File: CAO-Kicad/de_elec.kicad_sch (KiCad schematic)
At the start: 17 parts, among them J1 ICSP, SW1 COMMUTATEUR VIBRATION, U1 puce de microcontrôleur IC AT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

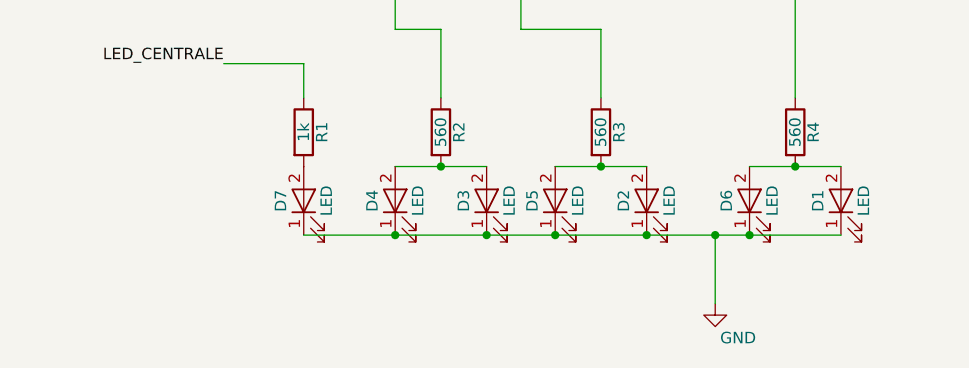
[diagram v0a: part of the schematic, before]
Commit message: Ajout de la serigraphie et recherche composants
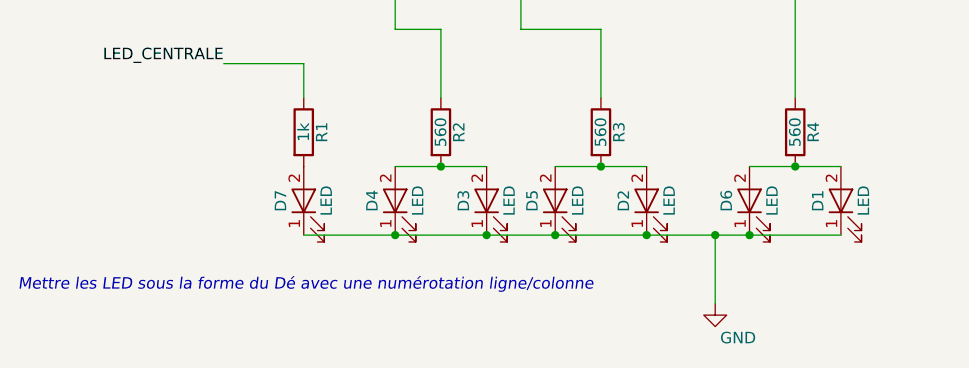
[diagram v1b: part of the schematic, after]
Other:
- note added: "Mettre les LED sous la forme du Dé avec une numérotation ligne/colonne"
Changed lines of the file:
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@@
     (stroke (width 0) (type solid) (color 0 0 0 0))
+  )
+  (text "Mettre les LED sous la forme du Dé avec une numérotation ligne/colonne"
+    (at 24.13 143.51 0)
+    (effects (font (size 1.27 1.27) italic) (justify left bottom))
   )
   (label "LED_CENTRALE" (at 46.99 118.11 180)

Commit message: Ajout des docs et images
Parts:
- removed D1, D2, D3, D4, D5, D6, D7: LED, LEDs:LED_D5.0mm, symbol kicad_dÚ-rescue:LED
- removed JP1: Jumper_2_Open, symbol Jumper:Jumper_2_Open
- removed R1: 1k, Resistors_SMD:R_0805_HandSoldering, symbol kicad_dÚ-rescue:R
- removed R2, R3, R4: 560, Resistors_SMD:R_0805_HandSoldering, symbol kicad_dÚ-rescue:R
- removed SW1: COMMUTATEUR VIBRATION, Capacitors_THT:CP_Radial_D5.0mm_P2.50mm, symbol kicad_dÚ-rescue:SW_SPST
- removed U1: puce de microcontrôleur IC ATTINY85 MCU 8BIT ATTI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, Housings_DIP:DIP-8_W7.62mm, symbol kicad_dÚ-rescue:ATTINY85-20PU
- added BT1: Battery_Cell_3V, symbol Device:Battery_Cell
- added D_L1C1, D_L1C3, D_L2C1, D_L2C2, D_L2C3, D_L3C1, D_L3C3: LED, symbol Device:LED
- added R1: 1k, symbol Device:R
- added R2, R3, R4: 560, symbol Device:R
- added SW1: COMMUTATEUR A BILLE, Capacitors_THT:CP_Radial_D5.0mm_P2.50mm, symbol Switch:SW_SPST
- added U1: ATtiny85V-10P, Package_DIP:DIP-8_W7.62mm, symbol MCU_Microchip_ATtiny:ATtiny85V-10P
- C1: value C -> 100n
- C2: value C_Polarized -> 10u
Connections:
- net GND: now also BT1.2 (-), D_L1C1.1 (K), D_L1C3.1 (K), D_L2C1.1 (K), D_L2C2.1 (K), D_L2C3.1 (K), D_L3C1.1 (K), D_L3C3.1 (K), SW1.2 (B), U1.4 (GND)
- net PB0/MOSI: now also R3.1, U1.5 (AREF/PB0)
- net PB1/MISO: now also R2.1, U1.6 (PB1)
- net PB2/SCK: now also SW1.1 (A), U1.7 (PB2)
- net PB5/RESET: now also U1.1 (~{RESET}/PB5)
- net VCC: now also BT1.1 (+), U1.8 (VCC)
- new net: R4.2, U1.3 (XTAL2/PB4)
- new net CMD_L2C2: R1.1, U1.2 (XTAL1/PB3)
- new net D_L1C1L3C3: D_L1C1.2 (A), D_L3C3.2 (A), R3.2
- new net D_L2C1C3: D_L2C1.2 (A), D_L2C3.2 (A), R4.1
- new net D_L2C2: D_L2C2.2 (A), R1.2
- new net D_L3C1L1C3: D_L1C3.2 (A), D_L3C1.2 (A), R2.2
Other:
- note added: "Carte microcontrôleur ATtiny85"
- note added: "Disposition des LED sous la forme du Dé avec une numérotation ligne/colonne"
- note added: "L1C1"
- note added: "L1C2"
- note added: "L1C3"
- note added: "L2C1"
- note added: "L2C2"
- note added: "L2C3"
- note added: "L3C1"
- note added: "L3C2"
- note added: "L3C3"
- note removed: "Mettre les LED sous la forme du Dé avec une numérotation ligne/colonne"
- moved on the sheet: C1, C2, J1

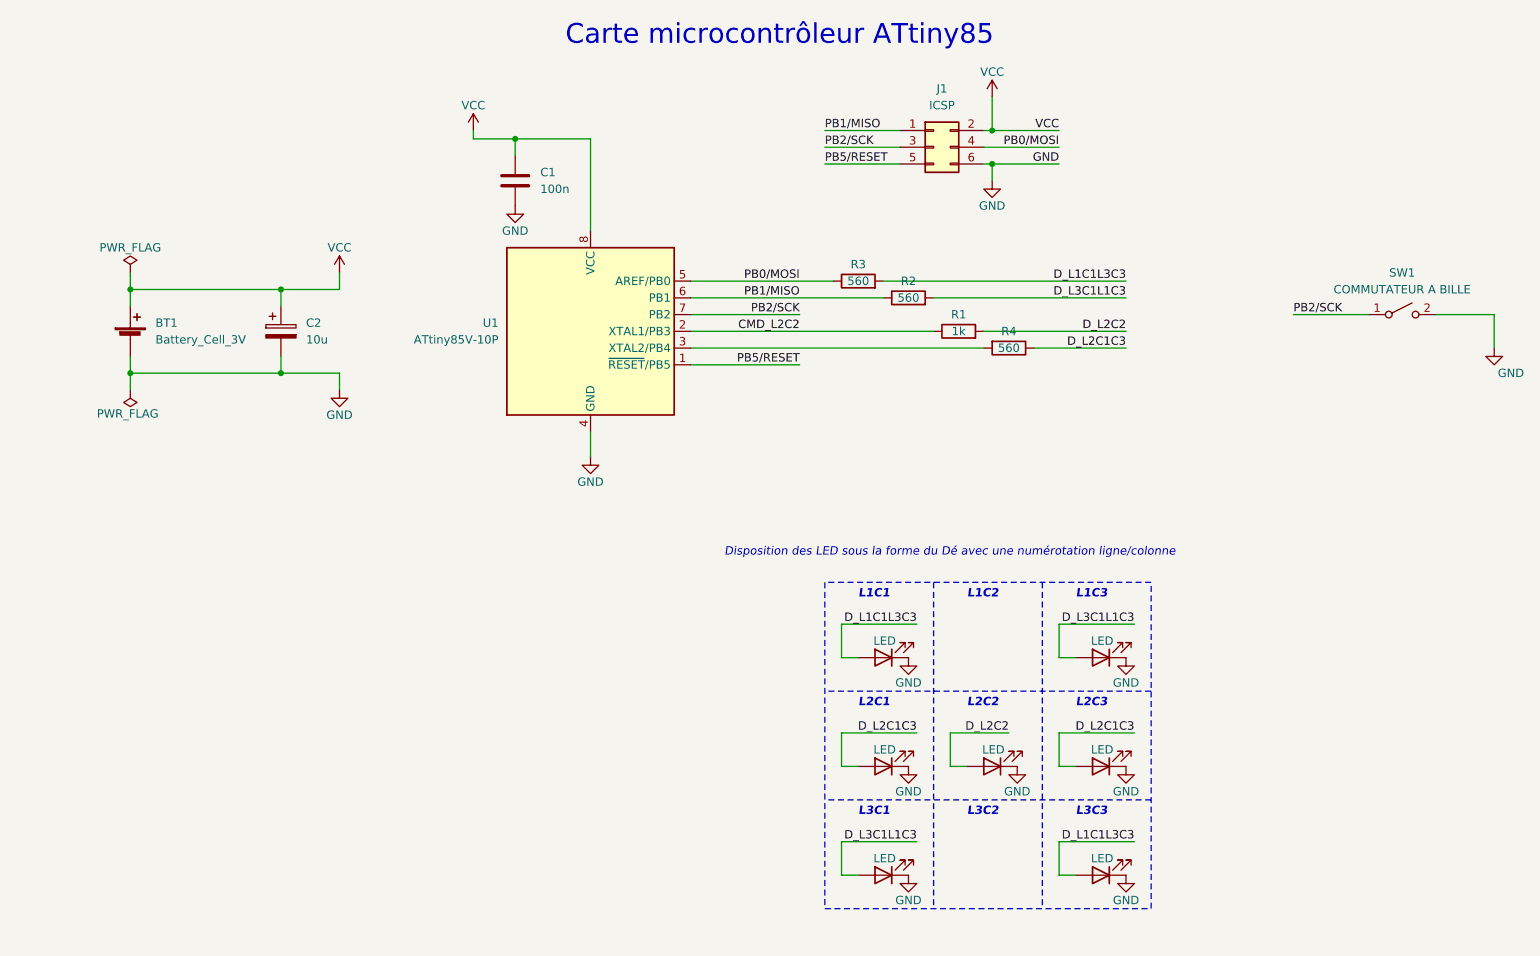
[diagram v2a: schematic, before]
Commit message: Importation des composants vers le circuit imprimé
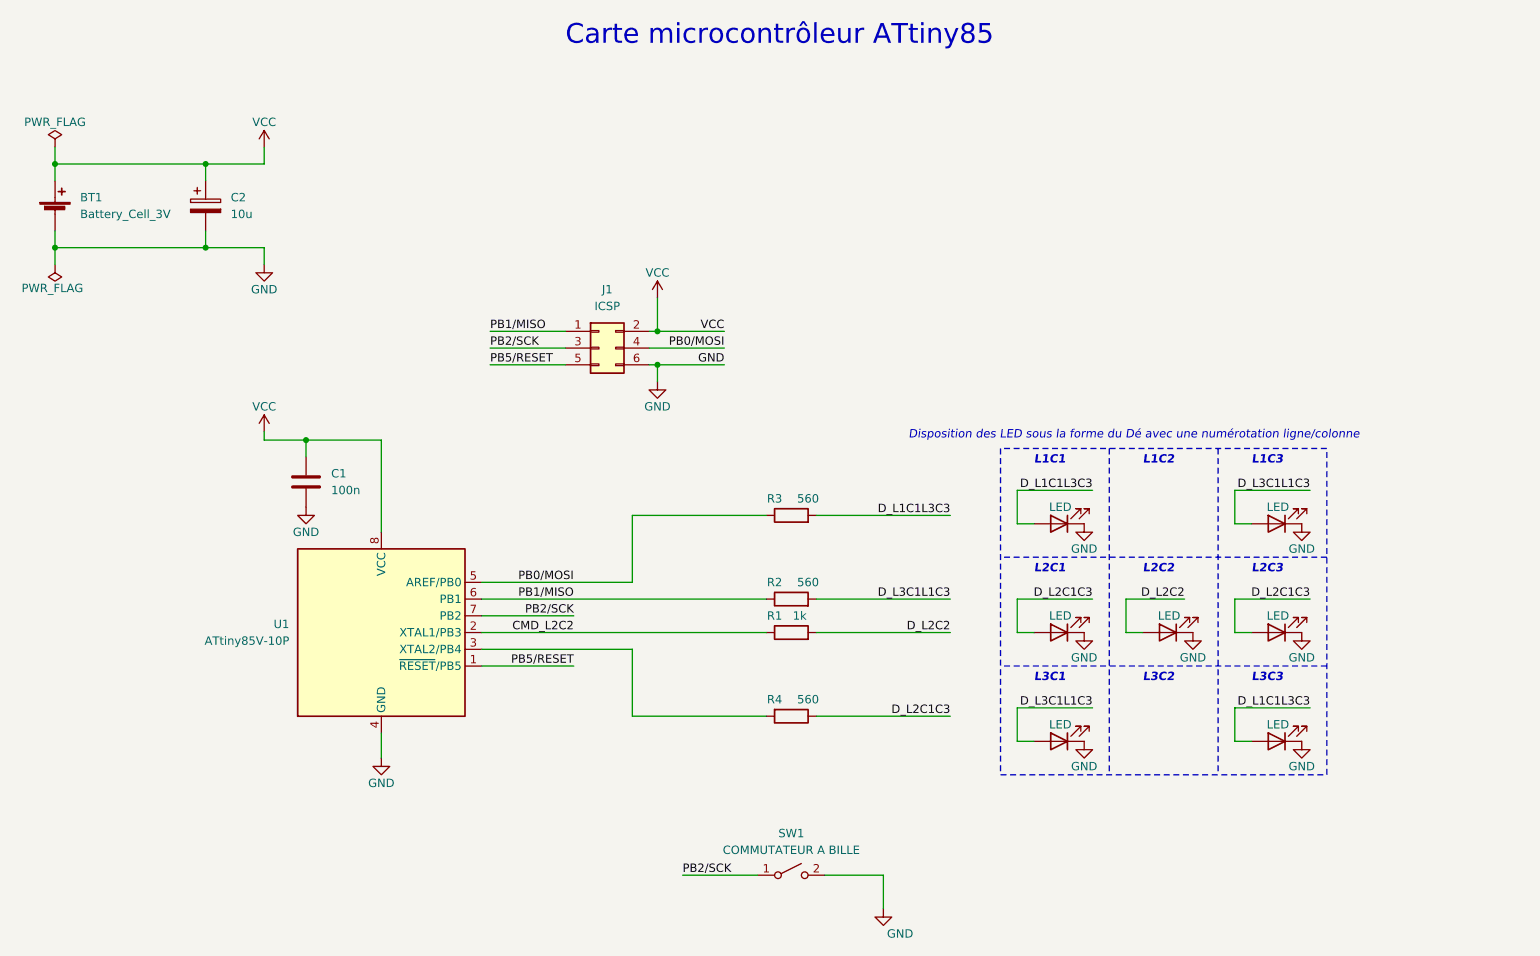
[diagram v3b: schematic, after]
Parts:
- BT1: footprint (none) -> Connector_PinHeader_2.54mm:PinHeader_1x02_P2.54mm_Vertical
- C1: footprint (none) -> Capacitor_THT:C_Rect_L7.2mm_W3.0mm_P5.00mm_FKS2_FKP2_MKS2_MKP2
- C2: footprint (none) -> Capacitor_THT:CP_Radial_D5.0mm_P2.50mm
- D_L1C1, D_L1C3, D_L2C1, D_L2C2, D_L2C3, D_L3C1, D_L3C3: footprint (none) -> LED_THT:LED_D5.0mm_Clear
- J1: footprint (none) -> Connector_PinHeader_2.54mm:PinHeader_2x03_P2.54mm_Vertical
- R1, R2, R3, R4: footprint (none) -> Resistor_THT:R_Axial_DIN0207_L6.3mm_D2.5mm_P10.16mm_Horizontal
- SW1: footprint Capacitors_THT:CP_Radial_D5.0mm_P2.50mm -> Capacitor_THT:CP_Radial_D4.0mm_P2.00mm
- U1: footprint Package_DIP:DIP-8_W7.62mm -> Package_DIP:DIP-8_W7.62mm_LongPads
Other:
- moved on the sheet: BT1, C1, C2, J1, R1, R2, R3, R4, SW1, U1
